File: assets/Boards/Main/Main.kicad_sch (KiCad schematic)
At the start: 9 parts, among them J1 PWR, J2 CTRLS_BOARD, U1 DFRobot_MAX98357, U2 Waveshare_ESP32-S3-Tiny

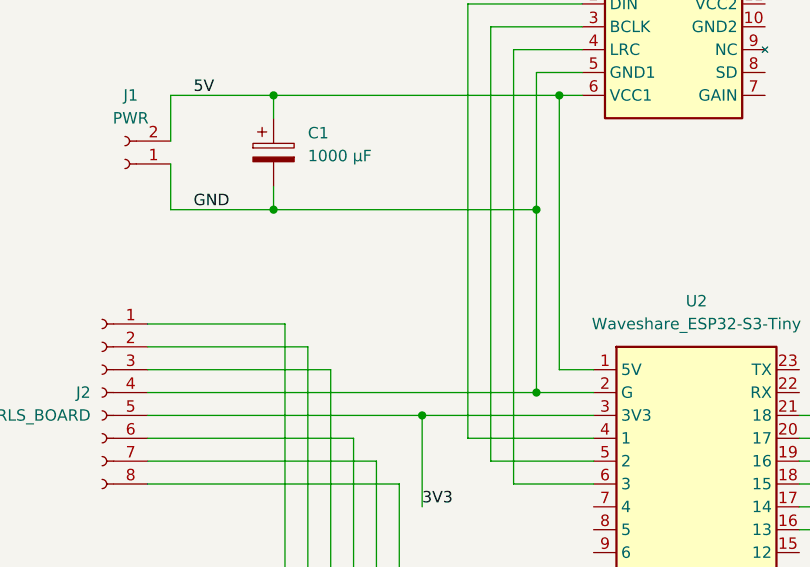
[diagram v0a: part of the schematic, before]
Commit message: Added ground plane, RF shield soldering points and text.
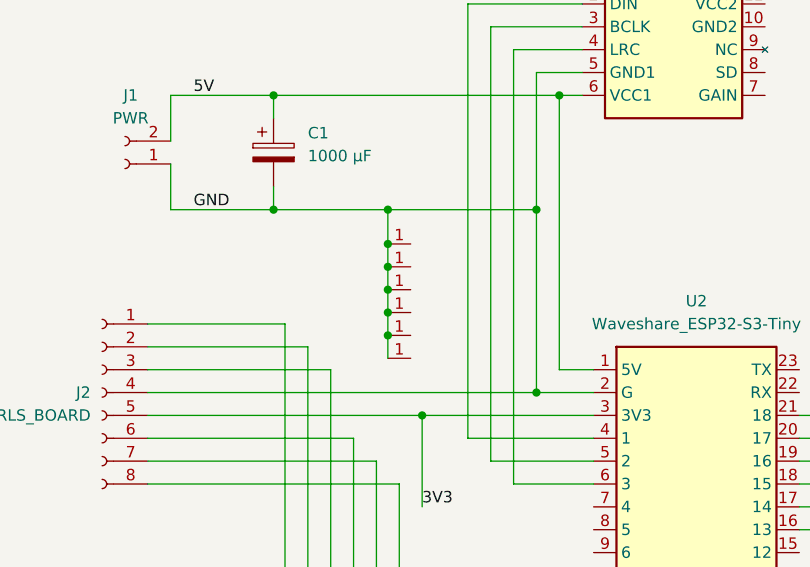
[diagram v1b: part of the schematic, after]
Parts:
- added U3, U4, U5, U6, U7, U8: ~, Custom Footprints:Solder pad 1.6x3.3mm, symbol Custom Symbols:Solder_pad
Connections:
- net GND: now also U3.1, U4.1, U5.1, U6.1, U7.1, U8.1

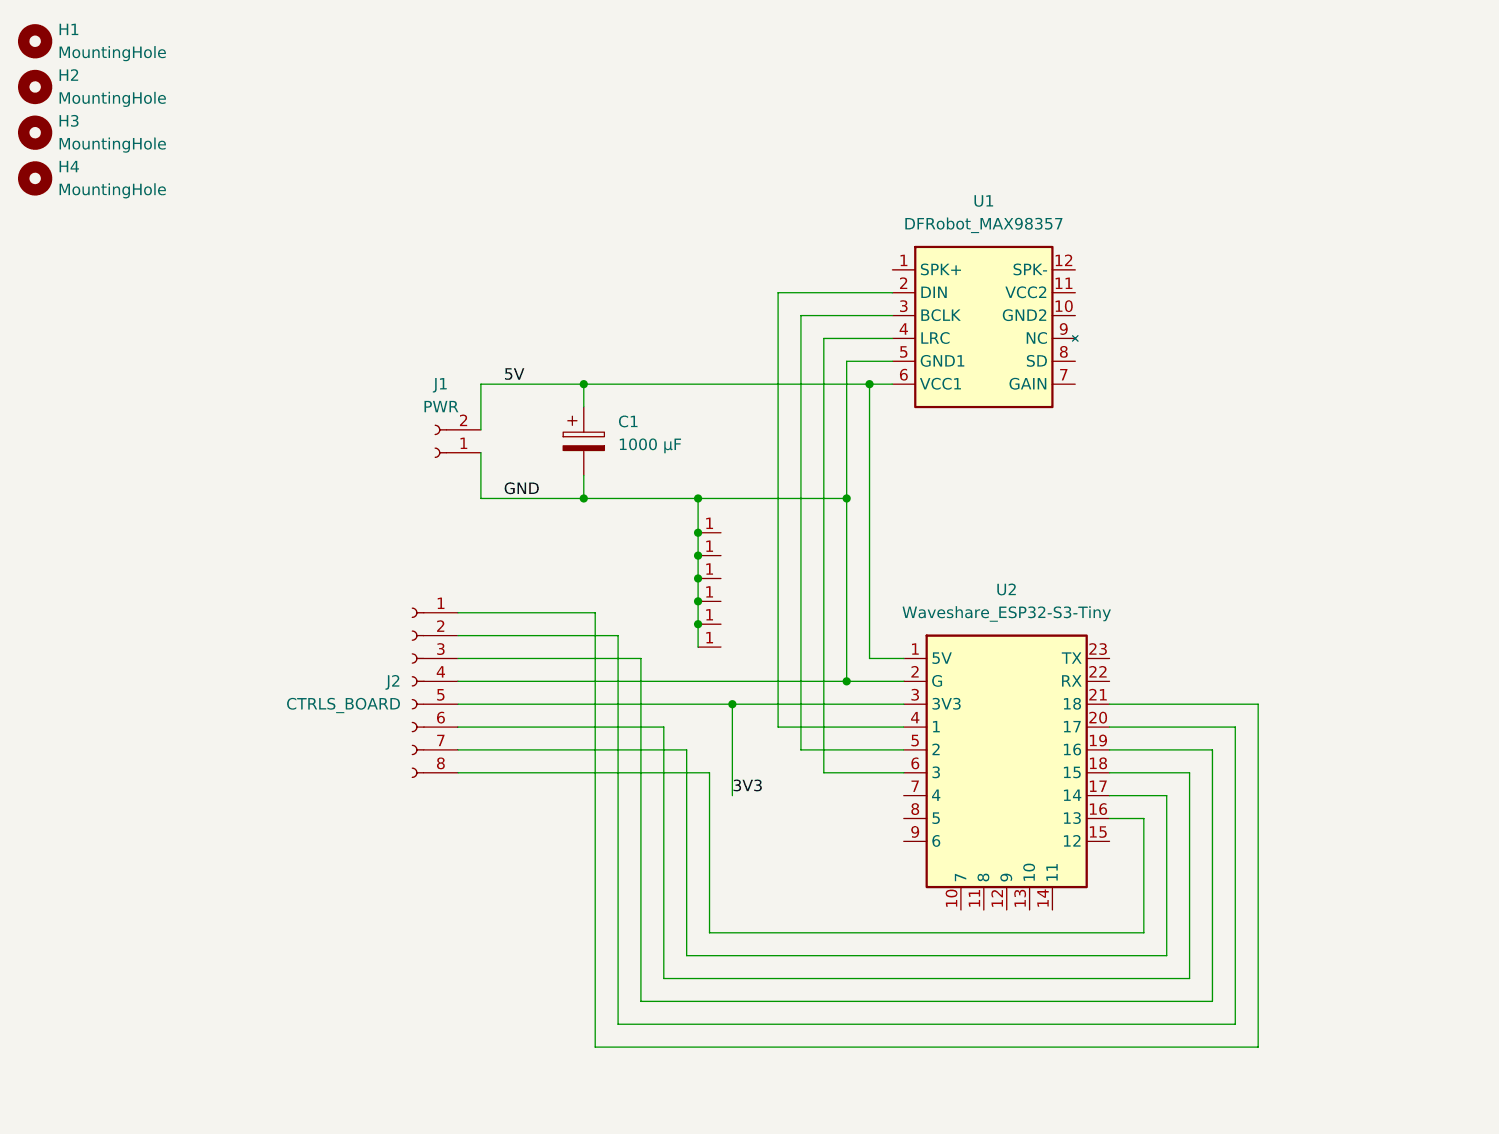
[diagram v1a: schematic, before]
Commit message: Reworked boards.
Added LDO for the mic. Changed layout of the main board to move the cap out of the way. Added ground and power plane. Added R33's for the signal lines of the mic.
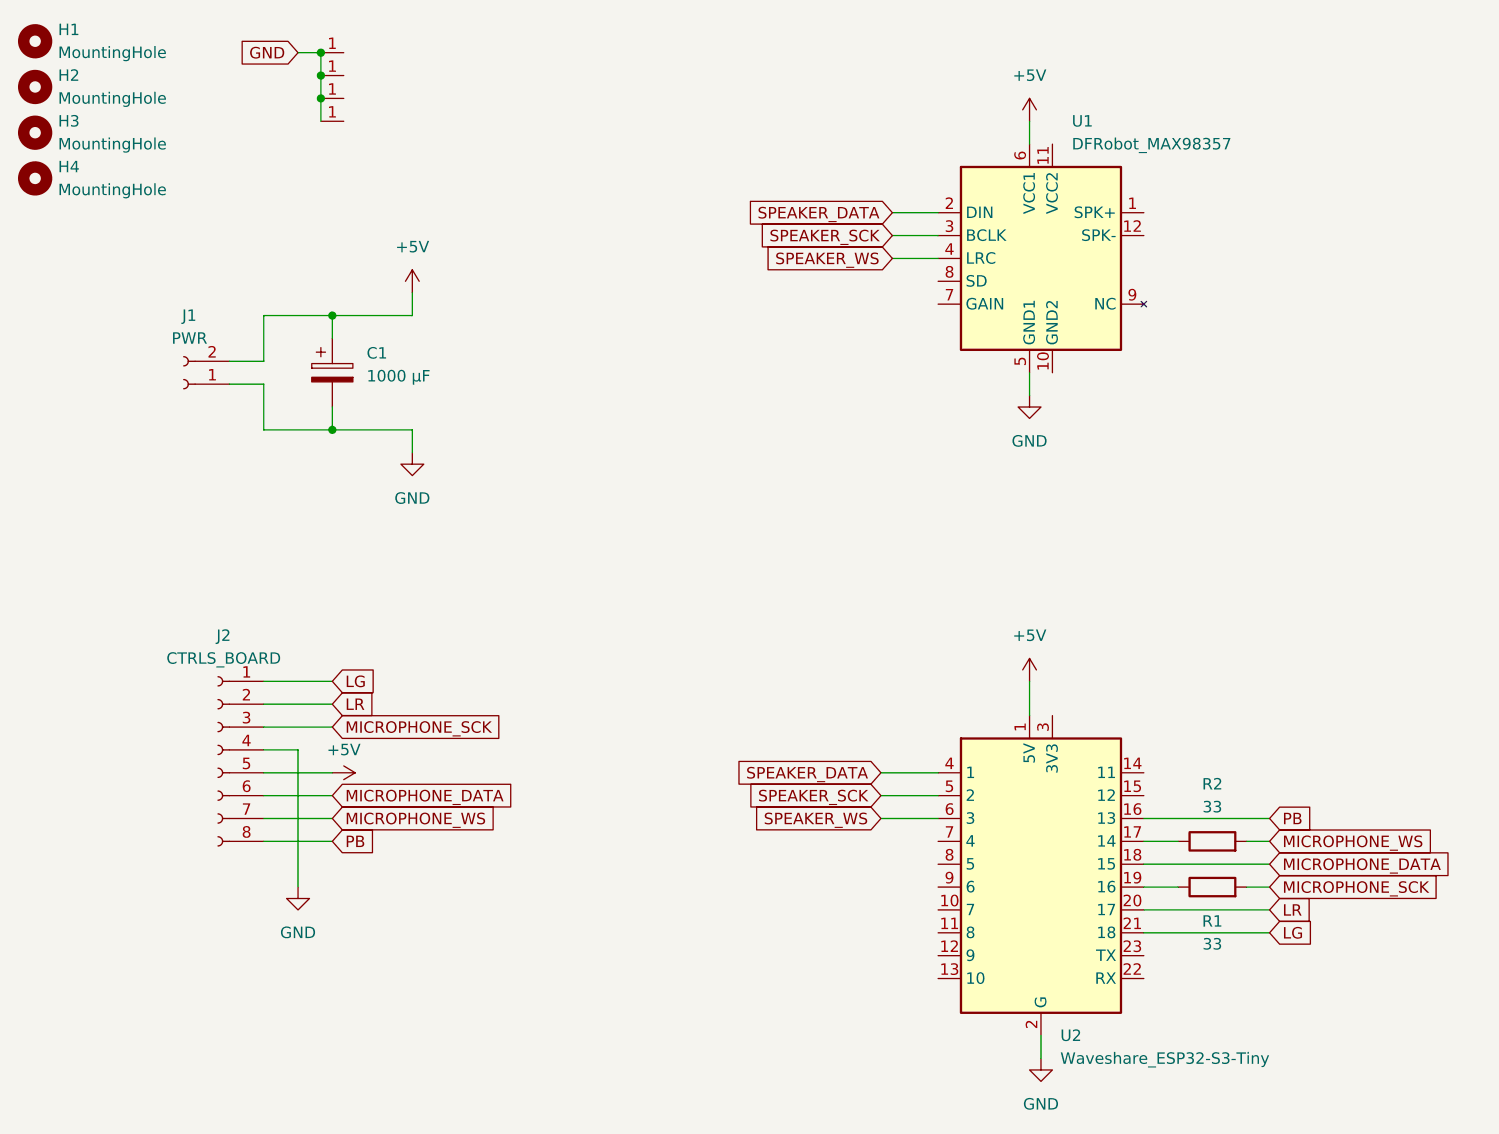
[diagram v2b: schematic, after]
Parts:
- removed U6, U7: ~, Custom Footprints:Solder pad 1.6x3.3mm, symbol Custom Symbols:Solder_pad
- added R1, R2: 33, Resistor_SMD:R_0805_2012Metric_Pad1.20x1.40mm_HandSolder, symbol Device:R
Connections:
- net PB: now reaches J2.8 (Pin_8), U2.16 (13)
- net at U2.17 (14): now also R2.1; no longer J2.7 (Pin_7)
- net MICROPHONE_DATA: now reaches J2.6 (Pin_6), U2.18 (15)
- net at U2.19 (16): now also R1.1; no longer J2.3 (Pin_3)
- net LR: now reaches J2.2 (Pin_2), U2.20 (17)
- net LG: now reaches J2.1 (Pin_1), U2.21 (18)
- net SPEAKER_DATA: now reaches U1.2 (DIN), U2.4 (1)
- net SPEAKER_SCK: now reaches U1.3 (BCLK), U2.5 (2)
- net SPEAKER_WS: now reaches U1.4 (LRC), U2.6 (3)
- net 3V3: no longer names the net of U2.3 (3V3)
- net 3V3: no longer J2.5 (Pin_5)
- net 5V renamed +5V
- net +5V: now also J2.5 (Pin_5)
- new net MICROPHONE_SCK: J2.3 (Pin_3), R1.2
- new net MICROPHONE_WS: J2.7 (Pin_7), R2.2
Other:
- moved on the sheet: C1, J1, J2, U1, U2

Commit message: Fixed ERC errors. Switched to double ground plane instead of ground and power plane. Switched to 1uF caps for the LDO conforming to the data sheet. Added logo.
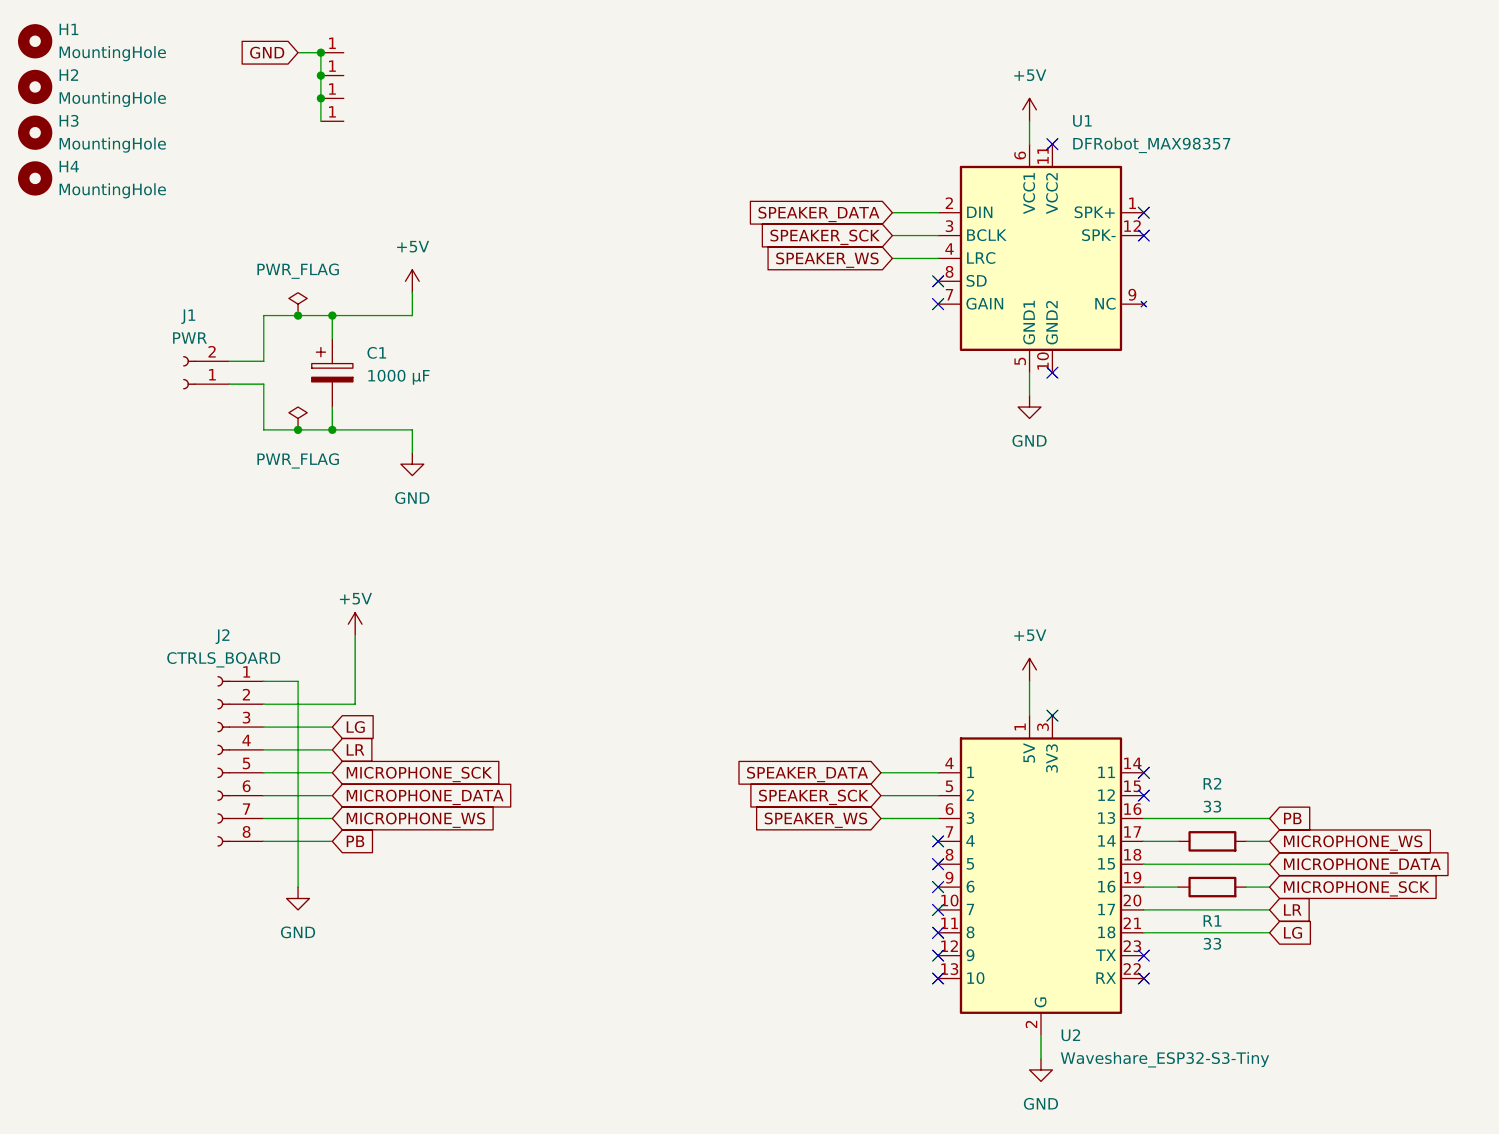
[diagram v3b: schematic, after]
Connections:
- net +5V: now also J2.2 (Pin_2); no longer J2.5 (Pin_5)
- net GND: now also J2.1 (Pin_1); no longer J2.4 (Pin_4)
- net LG: now also J2.3 (Pin_3); no longer J2.1 (Pin_1)
- net LR: now also J2.4 (Pin_4); no longer J2.2 (Pin_2)
- net MICROPHONE_SCK: now also J2.5 (Pin_5); no longer J2.3 (Pin_3)
- no-connect marks 0 -> 18

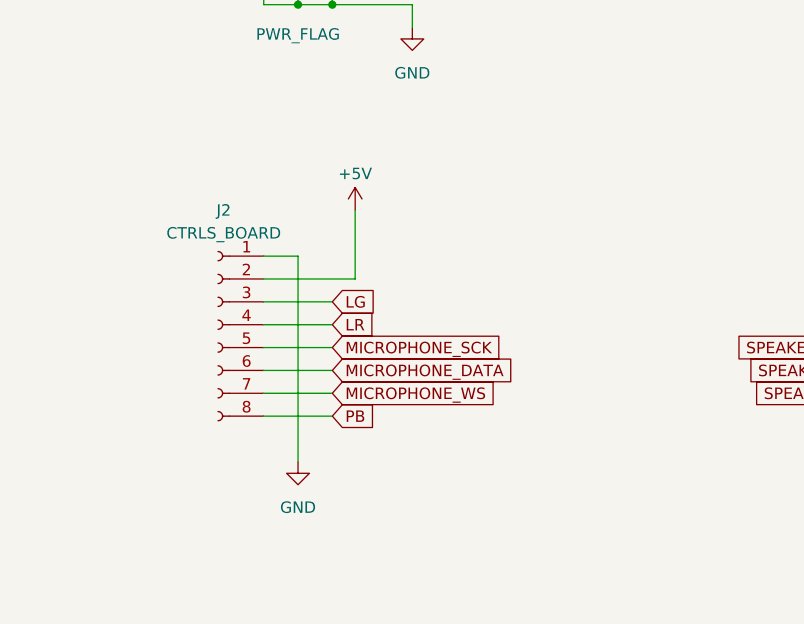
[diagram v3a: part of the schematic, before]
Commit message: Applied suggestions from Rick Hartley.
See https://www.youtube.com/watch?v=ySuUZEjARPY.
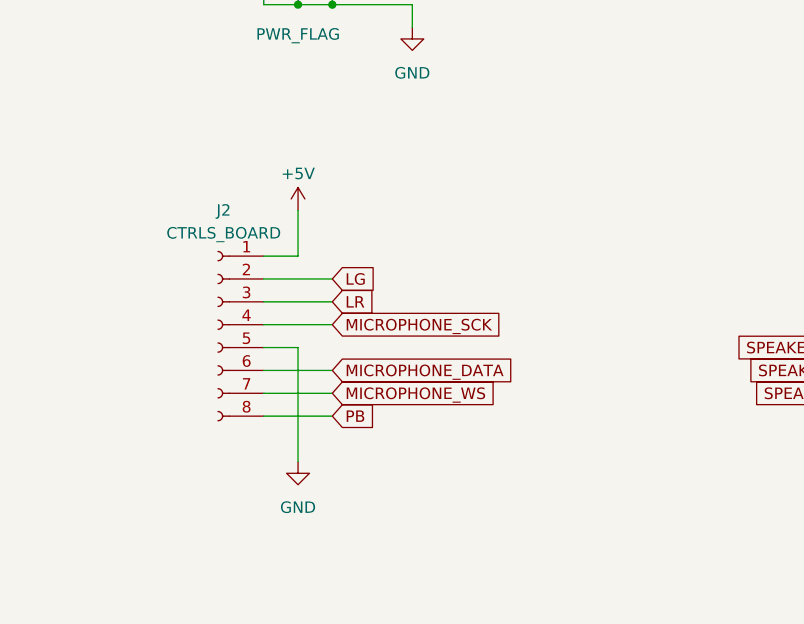
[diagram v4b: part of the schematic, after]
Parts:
- U1: footprint Custom Footprints:DFRobot_MAX98357 -> Custom Footprints:DFRobot_MAX98357_SMD
- U2: footprint Custom Footprints:Waveshare_ESP32-S3-Tiny -> Custom Footprints:Waveshare_ESP32-S3-Tiny_SMD
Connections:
- net +5V: now also J2.1 (Pin_1); no longer J2.2 (Pin_2)
- net GND: now also J2.5 (Pin_5); no longer J2.1 (Pin_1)
- net LG: now also J2.2 (Pin_2); no longer J2.3 (Pin_3)
- net LR: now also J2.3 (Pin_3); no longer J2.4 (Pin_4)
- net MICROPHONE_SCK: now also J2.4 (Pin_4); no longer J2.5 (Pin_5)
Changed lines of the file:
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@@
+	(wire
+		(pts
+			(xy 50.8 93.98) (xy 50.8 88.9)
+		)
+		(stroke
+			(width 0)
+			(type default)
+		)
+	)
 	(wire
 		(pts
@@
 	(wire
 		(pts
+			(xy 50.8 104.14) (xy 50.8 116.84)
+		)
+		(stroke
+			(width 0)
+			(type default)
+		)
+	)
+	(wire
+		(pts
 			(xy 144.78 119.38) (xy 158.75 119.38)
 		)
@@
 	(wire
 		(pts
+			(xy 54.61 66.04) (xy 63.5 66.04)
+		)
+		(stroke
+			(width 0)
+			(type default)
+		)
+	)
+	(wire
+		(pts
+			(xy 46.99 104.14) (xy 50.8 104.14)
+		)
+		(stroke
+			(width 0)
+			(type default)
+		)
+	)
+	(wire
+		(pts
 			(xy 46.99 93.98) (xy 50.8 93.98)
 		)
@@
 	(wire
 		(pts
-			(xy 54.61 66.04) (xy 63.5 66.04)
-		)
-		(stroke
-			(width 0)
-			(type default)
-		)
-	)
-	(wire
-		(pts
 			(xy 53.34 29.21) (xy 53.34 31.75)
 		)
@@
 	(wire
 		(pts
-			(xy 57.15 88.9) (xy 57.15 96.52)
-		)
-		(stroke
-			(width 0)
-			(type default)
-		)
-	)
-	(wire
-		(pts
 			(xy 132.08 62.23) (xy 132.08 59.69)
 		)
@@
 	(wire
 		(pts
-			(xy 54.61 104.14) (xy 46.99 104.14)
+			(xy 54.61 101.6) (xy 46.99 101.6)
 		)
 		(stroke
@@
 	(wire
 		(pts
-			(xy 46.99 101.6) (xy 54.61 101.6)
+			(xy 46.99 99.06) (xy 54.61 99.06)
 		)
 		(stroke
@@
 	(wire
 		(pts
-			(xy 50.8 93.98) (xy 50.8 116.84)
-		)
-		(stroke
-			(width 0)
-			(type default)
-		)
-	)
-	(wire
-		(pts
 			(xy 158.75 121.92) (xy 144.78 121.92)
 		)
@@
 	(wire
 		(pts
-			(xy 46.99 99.06) (xy 54.61 99.06)
+			(xy 46.99 96.52) (xy 54.61 96.52)
 		)
 		(stroke
@@
 		(pts
 			(xy 116.84 46.99) (xy 121.92 46.99)
-		)
-		(stroke
-			(width 0)
-			(type default)
-		)
-	)
-	(wire
-		(pts
-			(xy 57.15 96.52) (xy 46.99 96.52)
 		)
 		(stroke
@@
 	(global_label "LG"
 		(shape input)
-		(at 54.61 99.06 0)
+		(at 54.61 96.52 0)
 		(fields_autoplaced yes)
 		(effects
@@
 		)
 		(property "Intersheetrefs" "${INTERSHEET_REFS}"
-			(at 59.8933 99.06 0)
+			(at 59.8933 96.52 0)
 			(effects
 				(font
@@
 	(global_label "MICROPHONE_SCK"
 		(shape input)
-		(at 54.61 104.14 0)
+		(at 54.61 101.6 0)
 		(fields_autoplaced yes)
 		(effects
@@
 		)
 		(property "Intersheetrefs" "${INTERSHEET_REFS}"
-			(at 74.6495 104.14 0)
+			(at 74.6495 101.6 0)
 			(effects
 				(font
@@
 	(global_label "LR"
 		(shape input)
-		(at 54.61 101.6 0)
+		(at 54.61 99.06 0)
 		(fields_autoplaced yes)
 		(effects
@@
 		)
 		(property "Intersheetrefs" "${INTERSHEET_REFS}"
-			(at 59.8933 101.6 0)
+			(at 59.8933 99.06 0)
 			(effects
 				(font
@@
 			)
 		)
-		(property "Footprint" "Custom Footprints:Waveshare_ESP32-S3-Tiny"
+		(property "Footprint" "Custom Footprints:Waveshare_ESP32-S3-Tiny_SMD"
 			(at 134.62 125.73 0)
 			(effects
@@
 	(symbol
 		(lib_id "power:+5V")
-		(at 57.15 88.9 0)
+		(at 50.8 88.9 0)
 		(unit 1)
 		(exclude_from_sim no)
@@
 		(dnp no)
 		(property "Reference" "#PWR06"
-			(at 57.15 92.71 0)
+			(at 50.8 92.71 0)
 			(effects
 				(font
@@
 		)
 		(property "Value" "+5V"
-			(at 57.15 84.836 0)
+			(at 50.8 84.836 0)
 			(effects
 				(font
@@
 		)
 		(property "Footprint" ""
-			(at 57.15 88.9 0)
+			(at 50.8 88.9 0)
 			(effects
 				(font
@@
 		)
 		(property "Datasheet" ""
-			(at 57.15 88.9 0)
+			(at 50.8 88.9 0)
 			(effects
 				(font
@@
 		)
 		(property "Description" "Power symbol creates a global label with name \"+5V\""
-			(at 57.15 88.9 0)
+			(at 50.8 88.9 0)
 			(effects
 				(font
@@
 			)
 		)
-		(property "Footprint" "Custom Footprints:DFRobot_MAX98357"
+		(property "Footprint" "Custom Footprints:DFRobot_MAX98357_SMD"
 			(at 133.35 54.61 0)
 			(effects
